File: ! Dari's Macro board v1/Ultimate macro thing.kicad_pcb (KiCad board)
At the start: 2 copper layers, 71 parts, among them J1 Conn_02x03_Odd_Even, J2 Conn_01x04, SW1 SW_Push, SW2 SW_Push, SW3 Rotary_Encoder, U1 ATmega328P-PU, Y1 16Mhz

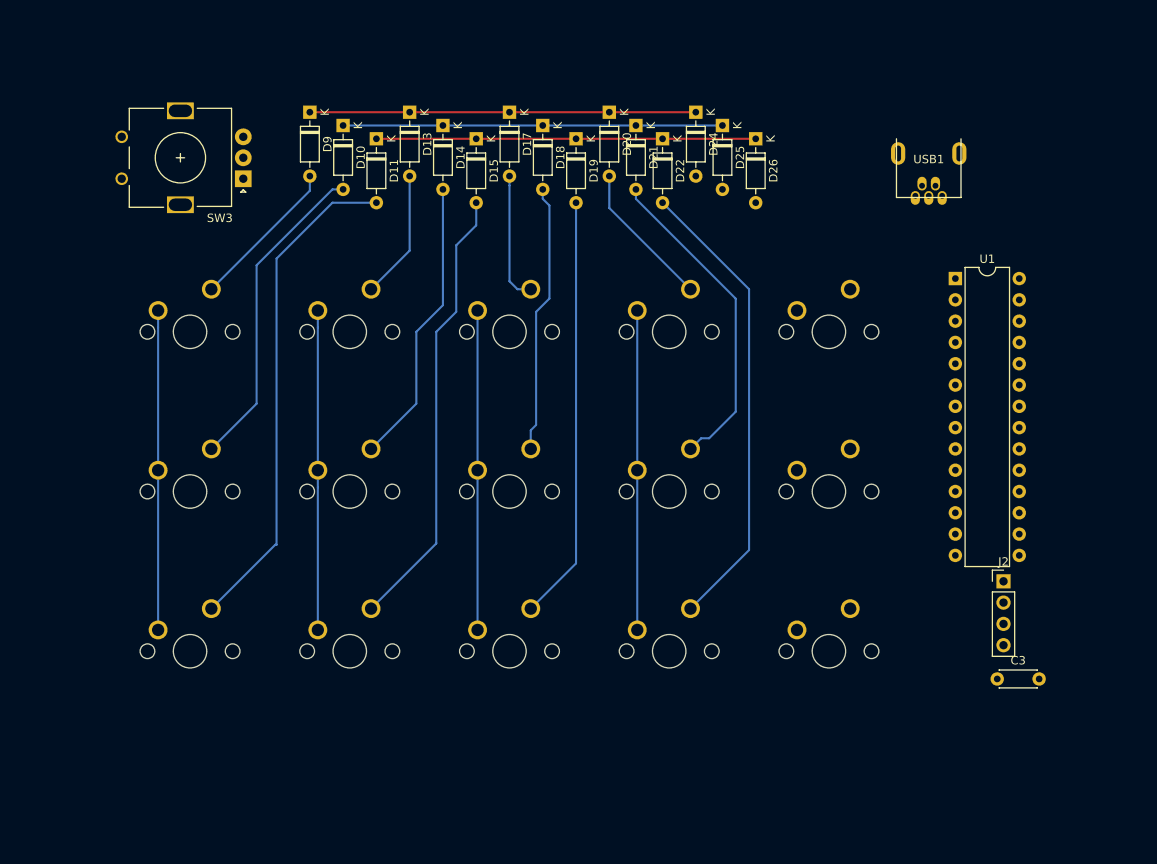
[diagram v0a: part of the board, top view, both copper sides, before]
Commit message: Linked encoder
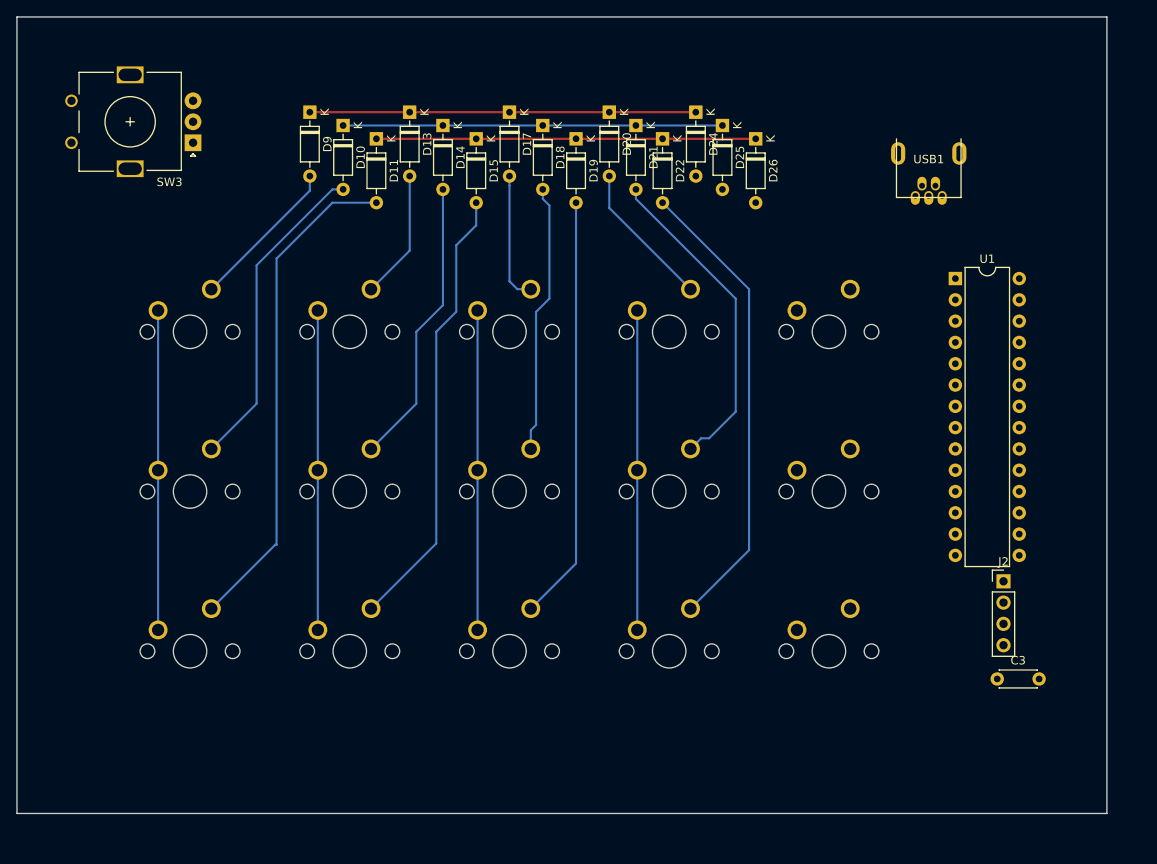
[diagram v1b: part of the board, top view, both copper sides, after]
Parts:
- moved SW3 7.37 mm to (71.0, 60.0)
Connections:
- SW3 pad A: Net-(SW3-PadA) -> ENC_A
- SW3 pad B: Net-(SW3-PadB) -> ENC_B
- SW3 pad C: Net-(SW3-PadC) -> ENC_C
- U1 pad 14: Net-(U1-Pad14) -> ENC_A
- U1 pad 15: Net-(U1-Pad15) -> ENC_C
- U1 pad 16: Net-(U1-Pad16) -> ENC_B
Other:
- board outline added: 130 x 95 mm
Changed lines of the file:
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@@
   (general
     (thickness 1.6)
-    (drawings 0)
+    (drawings 4)
     (tracks 72)
     (zones 0)
     (modules 71)
-    (nets 66)
+    (nets 63)
   )
   (page A4)
@@
     (solder_mask_min_width 0.25)
     (aux_axis_origin 0 0)
-    (visible_elements FFFFFF7F)
+    (visible_elements 7FFFFFFF)
     (pcbplotparams
       (layerselection 0x010fc_ffffffff)
@@
   (net 56 USB_D+)
   (net 57 "Net-(SW2-Pad1)")
-  (net 58 "Net-(SW3-PadA)")
-  (net 59 "Net-(SW3-PadC)")
-  (net 60 "Net-(SW3-PadB)")
-  (net 61 "Net-(U1-Pad14)")
-  (net 62 "Net-(U1-Pad21)")
-  (net 63 "Net-(U1-Pad16)")
-  (net 64 "Net-(U1-Pad15)")
-  (net 65 "Net-(USB1-Pad2)")
+  (net 58 "Net-(U1-Pad21)")
+  (net 59 "Net-(USB1-Pad2)")
+  (net 60 ENC_A)
+  (net 61 ENC_C)
+  (net 62 ENC_B)
   (net_class Default "This is the default net class."
     (clearance 0.2)
@@
     (add_net COL3)
     (add_net COL4)
+    (add_net ENC_A)
+    (add_net ENC_B)
+    (add_net ENC_C)
     (add_net GND)
     (add_net I2c_SCL)
@@
     (add_net "Net-(J1-Pad4)")
     (add_net "Net-(SW2-Pad1)")
-    (add_net "Net-(SW3-PadA)")
-    (add_net "Net-(SW3-PadB)")
-    (add_net "Net-(SW3-PadC)")
-    (add_net "Net-(U1-Pad14)")
-    (add_net "Net-(U1-Pad15)")
-    (add_net "Net-(U1-Pad16)")
     (add_net "Net-(U1-Pad21)")
     (add_net "Net-(USB1-Pad2)")
@@
       (net 6 "Net-(D2-Pad1)"))
     (pad 2 thru_hole oval (at 5.6 0.8 90) (size 1.65 1.1) (drill oval 0.7 (offset 0.25 0)) (layers *.Cu B.Mask)
-      (net 65 "Net-(USB1-Pad2)"))
+      (net 59 "Net-(USB1-Pad2)"))
     (pad 1 thru_hole oval (at 6.8 1.6 270) (size 1.65 1.1) (drill oval 0.7 (offset 0.25 0)) (layers *.Cu B.Mask)
       (net 1 GND))
@@
       (net 49 I2c_SCL))
     (pad 14 thru_hole oval (at 0 33.02) (size 1.6 1.6) (drill 0.8) (layers *.Cu *.Mask)
-      (net 61 "Net-(U1-Pad14)"))
+      (net 60 ENC_A))
     (pad 27 thru_hole oval (at 7.62 2.54) (size 1.6 1.6) (drill 0.8) (layers *.Cu *.Mask)
       (net 48 I2c_SDA))
@@
       (net 1 GND))
     (pad 21 thru_hole oval (at 7.62 17.78) (size 1.6 1.6) (drill 0.8) (layers *.Cu *.Mask)
-      (net 62 "Net-(U1-Pad21)"))
+      (net 58 "Net-(U1-Pad21)"))
     (pad 7 thru_hole oval (at 0 15.24) (size 1.6 1.6) (drill 0.8) (layers *.Cu *.Mask)
       (net 2 +5V))
@@
       (net 52 COL2))
     (pad 16 thru_hole oval (at 7.62 30.48) (size 1.6 1.6) (drill 0.8) (layers *.Cu *.Mask)
-      (net 63 "Net-(U1-Pad16)"))
+      (net 62 ENC_B))
     (pad 2 thru_hole oval (at 0 2.54) (size 1.6 1.6) (drill 0.8) (layers *.Cu *.Mask)
       (net 51 COL1))
     (pad 15 thru_hole oval (at 7.62 33.02) (size 1.6 1.6) (drill 0.8) (layers *.Cu *.Mask)
-      (net 64 "Net-(U1-Pad15)"))
+      (net 61 ENC_C))
     (pad 1 thru_hole rect (at 0 0) (size 1.6 1.6) (drill 0.8) (layers *.Cu *.Mask)
       (net 44 Reset))
@@
   )
   (module Rotary_Encoder:RotaryEncoder_Alps_EC11E_Vertical_H20mm (layer F.Cu)
-    (at 76.99375 64.29375 180)
+    (at 71 60 180)
     (descr "Alps rotary encoder, EC12E... without switch (pins are dummy), vertical shaft, http://www.alps.com/prod/info/E/HTML/Encoder/Incremental/EC11/EC11E15204A3.html")
     (tags "rotary encoder")
@@
     )
     (pad A thru_hole rect (at 0 0 180) (size 2 2) (drill 1) (layers *.Cu *.Mask)
-      (net 58 "Net-(SW3-PadA)"))
+      (net 60 ENC_A))
     (pad C thru_hole circle (at 0 2.5 180) (size 2 2) (drill 1) (layers *.Cu *.Mask)
-      (net 59 "Net-(SW3-PadC)"))
+      (net 61 ENC_C))
     (pad B thru_hole circle (at 0 5 180) (size 2 2) (drill 1) (layers *.Cu *.Mask)
-      (net 60 "Net-(SW3-PadB)"))
+      (net 62 ENC_B))
     (pad MP thru_hole rect (at 7.5 -3.1 180) (size 3.2 2) (drill oval 2.8 1.5) (layers *.Cu *.Mask))
     (pad MP thru_hole rect (at 7.5 8.1 180) (size 3.2 2) (drill oval 2.8 1.5) (layers *.Cu *.Mask))
@@
     )
   )
+  (gr_line (start 180 45) (end 180 140) (layer Edge.Cuts) (width 0.05))
+  (gr_line (start 50 140) (end 50 45) (layer Edge.Cuts) (width 0.05))
+  (gr_line (start 180 140) (end 50 140) (layer Edge.Cuts) (width 0.05))
+  (gr_line (start 50 45) (end 180 45) (layer Edge.Cuts) (width 0.05))
   (segment (start 84.93125 65.7225) (end 73.18375 77.47) (width 0.25) (layer B.Cu) (net 14))
   (segment (start 84.93125 63.97625) (end 84.93125 65.7225) (width 0.25) (layer B.Cu) (net 14))

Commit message: Redesign
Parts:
- removed D10, D11, D26, D9: 1N4148, Diode_THT:D_DO-35_SOD27_P7.62mm_Horizontal
- removed D12, D16, D27, D28, D29, D30, D31, D32, D33, D34, D8: WS2812B, LED_SMD:LED_WS2812B_PLCC4_5.0x5.0mm_P3.2mm
- added R10: 220, Resistor_THT:R_Axial_DIN0204_L3.6mm_D1.6mm_P5.08mm_Horizontal, F.Cu at (309.8, 229.9)
- added R9: 220, Resistor_THT:R_Axial_DIN0204_L3.6mm_D1.6mm_P5.08mm_Horizontal, F.Cu at (309.8, 226.8)
- D23, D7: value WS2812B -> 1N4148; footprint LED_SMD:LED_WS2812B_PLCC4_5.0x5.0mm_P3.2mm -> Diode_THT:D_DO-35_SOD27_P7.62mm_Horizontal
- D3: value WS2812B -> RED; footprint LED_SMD:LED_WS2812B_PLCC4_5.0x5.0mm_P3.2mm -> LED_THT:LED_D3.0mm_Clear
- D4: value WS2812B -> GREEN; footprint LED_SMD:LED_WS2812B_PLCC4_5.0x5.0mm_P3.2mm -> LED_THT:LED_D3.0mm_Clear
- D5: value RED -> 1N4148; footprint LED_THT:LED_D3.0mm_Clear -> Diode_THT:D_DO-35_SOD27_P7.62mm_Horizontal
- D6: value GREEN -> 1N4148; footprint LED_THT:LED_D3.0mm_Clear -> Diode_THT:D_DO-35_SOD27_P7.62mm_Horizontal
- MX10, MX12, MX14, MX3, MX4, MX8: footprint ! MX bases:MXOnly-1U-NoLED -> ! MX bases:MXOnly-1U
- moved D14 255.1 mm to (354.3, 86.9), turned to 0 degrees
- moved D15 226.1 mm to (323.3, 117.7), turned to 0 degrees
- moved D20 226.0 mm to (343.5, 94.0), turned to 0 degrees
- moved MX15 222.0 mm to (269.0, 287.0)
- moved D22 219.8 mm to (343.5, 97.5), turned to 0 degrees
- moved U1 216.1 mm to (289.0, 251.0)
- moved MX1 206.6 mm to (193.0, 249.0)
- moved MX4 206.6 mm to (212.0, 249.0)
- moved MX2 206.5 mm to (193.0, 268.0)
- moved MX7 206.5 mm to (231.0, 249.0)
- moved MX5 206.5 mm to (212.0, 268.0)
- moved MX3 206.5 mm to (193.0, 287.0)
- moved MX10 206.5 mm to (250.0, 249.0)
- moved MX8 206.5 mm to (231.0, 268.0)
- moved MX6 206.5 mm to (212.0, 287.0)
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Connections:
- D23 pad 1: +5V -> ROW0
- D24 pad 1: ROW0 -> ROW1
- D25 pad 1: ROW1 -> ROW2
- D3 pad 1: +5V -> GND
- D4 pad 1: +5V -> GND
- D5 pad 1: GND -> ROW0
- D6 pad 1: GND -> ROW1
- D7 pad 1: +5V -> ROW2
- J1 pad 3: Net-(J1-Pad3) -> ROW0
- MX1 pad 2: Net-(D9-Pad2) -> Net-(D5-Pad2)
- MX13 pad 2: Net-(D24-Pad2) -> Net-(D23-Pad2)
- MX14 pad 2: Net-(D25-Pad2) -> Net-(D24-Pad2)
- MX15 pad 2: Net-(D26-Pad2) -> Net-(D25-Pad2)
- MX2 pad 2: Net-(D10-Pad2) -> Net-(D6-Pad2)
- MX3 pad 2: Net-(D11-Pad2) -> Net-(D7-Pad2)
- R5 pad 1: Net-(D5-Pad2) -> Net-(D3-Pad2)
- R6 pad 1: Net-(D6-Pad2) -> Net-(D4-Pad2)
- U1 pad 19: Net-(J1-Pad3) -> ROW0
- U1 pad 23: ROW0 -> LED1
- U1 pad 6: RGBINPUT -> LED2
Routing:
- net Net-(D11-Pad2): track 59.7 -> 0.00 mm
- net Net-(D22-Pad2): track 55.6 -> 0.00 mm
- net Net-(D15-Pad2): track 53.6 -> 0.00 mm
- net Net-(D19-Pad2): track 50.7 -> 0.00 mm
- net ROW0: track 46.0 -> 0.00 mm
- net ROW2: track 45.2 -> 0.00 mm
- net ROW1: track 45.2 -> 0.00 mm
- net Net-(D21-Pad2): track 39.6 -> 0.00 mm
- net Net-(D10-Pad2): track 38.2 -> 0.00 mm
- net COL3: track 38.1 -> 0.00 mm
- net COL2: track 38.1 -> 0.00 mm
- net COL1: track 38.1 -> 0.00 mm
- net COL0: track 38.1 -> 0.00 mm
- net Net-(D14-Pad2): track 34.5 -> 0.00 mm
- net Net-(D18-Pad2): track 32.5 -> 0.00 mm
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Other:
- board outline removed

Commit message: Redesigned pro micro
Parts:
- removed R10: 220, Resistor_THT:R_Axial_DIN0204_L3.6mm_D1.6mm_P5.08mm_Horizontal
- added D10: 1N4148, Diode_THT:D_DO-35_SOD27_P7.62mm_Horizontal, F.Cu at (400.7, 417.6)
- added D11: 1N4148, Diode_THT:D_DO-35_SOD27_P7.62mm_Horizontal, F.Cu at (400.7, 414.1)
- added D12: 1N4148, Diode_THT:D_DO-35_SOD27_P7.62mm_Horizontal, F.Cu at (389.9, 421.2)
- added D16: 1N4148, Diode_THT:D_DO-35_SOD27_P7.62mm_Horizontal, F.Cu at (369.5, 425.4)
- added D26: 1N4148, Diode_THT:D_DO-35_SOD27_P7.62mm_Horizontal, F.Cu at (412.6, 424.7)
- added D27: 1N4148, Diode_THT:D_DO-35_SOD27_P7.62mm_Horizontal, F.Cu at (500.2, 336.8)
- added D28: 1N4148, Diode_THT:D_DO-35_SOD27_P7.62mm_Horizontal, F.Cu at (422.2, 414.1)
- added D29: WS2812B, LED_SMD:LED_WS2812B_PLCC4_5.0x5.0mm_P3.2mm, F.Cu at (480.2, 381.8)
- added D30: WS2812B, LED_SMD:LED_WS2812B_PLCC4_5.0x5.0mm_P3.2mm, F.Cu at (513.4, 351.1)
- added D31: WS2812B, LED_SMD:LED_WS2812B_PLCC4_5.0x5.0mm_P3.2mm, F.Cu at (500.4, 360.6)
- added D32: WS2812B, LED_SMD:LED_WS2812B_PLCC4_5.0x5.0mm_P3.2mm, F.Cu at (492.0, 358.6)
- added D33: WS2812B, LED_SMD:LED_WS2812B_PLCC4_5.0x5.0mm_P3.2mm, F.Cu at (460.0, 402.0)
- added D34: WS2812B, LED_SMD:LED_WS2812B_PLCC4_5.0x5.0mm_P3.2mm, F.Cu at (471.8, 378.8)
- added D35: WS2812B, LED_SMD:LED_WS2812B_PLCC4_5.0x5.0mm_P3.2mm, F.Cu at (451.6, 399.0)
- added D36: WS2812B, LED_SMD:LED_WS2812B_PLCC4_5.0x5.0mm_P3.2mm, F.Cu at (462.4, 395.4)
- added D37: WS2812B, LED_SMD:LED_WS2812B_PLCC4_5.0x5.0mm_P3.2mm, F.Cu at (451.6, 405.6)
- added D38: WS2812B, LED_SMD:LED_WS2812B_PLCC4_5.0x5.0mm_P3.2mm, F.Cu at (471.8, 385.4)
- added D39: WS2812B, LED_SMD:LED_WS2812B_PLCC4_5.0x5.0mm_P3.2mm, F.Cu at (492.0, 365.2)
- added D40: WS2812B, LED_SMD:LED_WS2812B_PLCC4_5.0x5.0mm_P3.2mm, F.Cu at (502.9, 354.0)
- added D41: WS2812B, LED_SMD:LED_WS2812B_PLCC4_5.0x5.0mm_P3.2mm, F.Cu at (482.6, 375.2)
- added D42: WS2812B, LED_SMD:LED_WS2812B_PLCC4_5.0x5.0mm_P3.2mm, F.Cu at (513.6, 344.5)
- added D43: WS2812B, LED_SMD:LED_WS2812B_PLCC4_5.0x5.0mm_P3.2mm, F.Cu at (435.6, 424.2)
- added D44: WS2812B, LED_SMD:LED_WS2812B_PLCC4_5.0x5.0mm_P3.2mm, F.Cu at (446.2, 415.6)
- added D45: WS2812B, LED_SMD:LED_WS2812B_PLCC4_5.0x5.0mm_P3.2mm, F.Cu at (454.6, 412.2)
- added D46: WS2812B, LED_SMD:LED_WS2812B_PLCC4_5.0x5.0mm_P3.2mm, F.Cu at (471.8, 392.0)
- added D47: WS2812B, LED_SMD:LED_WS2812B_PLCC4_5.0x5.0mm_P3.2mm, F.Cu at (492.0, 371.8)
- added D48: WS2812B, LED_SMD:LED_WS2812B_PLCC4_5.0x5.0mm_P3.2mm, F.Cu at (444.0, 424.2)
- added D49: WS2812B, LED_SMD:LED_WS2812B_PLCC4_5.0x5.0mm_P3.2mm, F.Cu at (500.4, 367.3)
- added D50: WS2812B, LED_SMD:LED_WS2812B_PLCC4_5.0x5.0mm_P3.2mm, F.Cu at (480.2, 388.5)
- added D51: WS2812B, LED_SMD:LED_WS2812B_PLCC4_5.0x5.0mm_P3.2mm, F.Cu at (508.9, 360.6)
- added D52: WS2812B, LED_SMD:LED_WS2812B_PLCC4_5.0x5.0mm_P3.2mm, F.Cu at (468.5, 402.0)
- added D8: 1N4148, Diode_THT:D_DO-35_SOD27_P7.62mm_Horizontal, F.Cu at (489.4, 353.5)
- added D9: 1N4148, Diode_THT:D_DO-35_SOD27_P7.62mm_Horizontal, F.Cu at (391.1, 424.7)
- added MX16: MX-NoLED, ! MX bases:MXOnly-1U-NoLED, F.Cu at (367.4, 341.6)
- added MX17: MX-NoLED, ! MX bases:MXOnly-1U-NoLED, F.Cu at (356.5, 399.0)
- added MX18: MX-NoLED, ! MX bases:MXOnly-1U-NoLED, F.Cu at (387.6, 341.6)
- added MX19: MX-NoLED, ! MX bases:MXOnly-1U-NoLED, F.Cu at (376.7, 361.8)
- added MX20: MX-NoLED, ! MX bases:MXOnly-1U-NoLED, F.Cu at (407.8, 341.6)
- added MX21: MX-NoLED, ! MX bases:MXOnly-1U-NoLED, F.Cu at (428.0, 341.6)
- added MX22: MX-NoLED, ! MX bases:MXOnly-1U-NoLED, F.Cu at (396.9, 361.8)
- added MX23: MX-NoLED, ! MX bases:MXOnly-1U-NoLED, F.Cu at (376.7, 382.0)
- added MX24: MX-NoLED, ! MX bases:MXOnly-1U-NoLED, F.Cu at (417.1, 361.8)
- MX10, MX12, MX14, MX3, MX4, MX8: footprint ! MX bases:MXOnly-1U -> ! MX bases:MXOnly-1U-NoLED
- R9: value 220 -> 470
- moved C2 345.2 mm to (423.4, 424.7)
- moved D4 341.6 mm to (449.9, 424.8)
- moved D5 341.1 mm to (411.4, 421.2)
- moved D2 339.3 mm to (401.8, 424.7)
- moved SW1 333.1 mm to (433.4, 414.3)
- moved D14 329.1 mm to (389.9, 414.1)
- moved D22 328.4 mm to (358.8, 425.6)
- moved D25 322.8 mm to (422.2, 417.6)
- moved D6 322.8 mm to (411.4, 417.6)
- moved R7 318.7 mm to (449.7, 420.5)
- moved R1 316.0 mm to (457.3, 406.9)
- moved D3 315.7 mm to (460.5, 411.3)
- moved R5 315.1 mm to (477.5, 393.3)
- moved R4 313.3 mm to (468.1, 396.9)
- moved D15 312.9 mm to (380.3, 425.4)
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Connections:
- net LED1 renamed RGBINPUT
- net Net-(J1-Pad1) renamed /COL5
- D20 pad 1: ROW0 -> /ROW3
- D21 pad 1: ROW1 -> ROW0
- D22 pad 1: ROW2 -> ROW1
- D23 pad 1: ROW0 -> ROW2
- D24 pad 1: ROW1 -> /ROW3
- D25 pad 1: ROW2 -> ROW0
- J1 pad 3: ROW0 -> /ROW3
- MX10 pad 1: COL3 -> COL2
- MX10 pad 2: Net-(D20-Pad2) -> Net-(D14-Pad2)
- MX11 pad 1: COL3 -> COL2
- MX11 pad 2: Net-(D21-Pad2) -> Net-(D15-Pad2)
- MX12 pad 1: COL3 -> COL2
- MX12 pad 2: Net-(D22-Pad2) -> Net-(D16-Pad2)
- MX13 pad 1: COL4 -> COL3
- MX13 pad 2: Net-(D23-Pad2) -> Net-(D17-Pad2)
- MX14 pad 1: COL4 -> COL3
- MX14 pad 2: Net-(D24-Pad2) -> Net-(D18-Pad2)
- MX15 pad 1: COL4 -> COL3
- MX15 pad 2: Net-(D25-Pad2) -> Net-(D19-Pad2)
- MX4 pad 1: COL1 -> COL0
- MX4 pad 2: Net-(D13-Pad2) -> Net-(D8-Pad2)
- MX5 pad 2: Net-(D14-Pad2) -> Net-(D9-Pad2)
- MX6 pad 2: Net-(D15-Pad2) -> Net-(D10-Pad2)
- MX7 pad 1: COL2 -> COL1
- MX7 pad 2: Net-(D17-Pad2) -> Net-(D11-Pad2)
- MX8 pad 1: COL2 -> COL1
- MX8 pad 2: Net-(D18-Pad2) -> Net-(D12-Pad2)
- MX9 pad 2: Net-(D19-Pad2) -> Net-(D13-Pad2)
- R9 pad 1: Net-(MX10-Pad3) -> Net-(D29-Pad4)
- U1 pad 19: ROW0 -> /ROW3
- U1 pad 6: LED2 -> ROW0

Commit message: a
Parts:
- moved SW3 235.4 mm to (334.0, 179.0), turned to 180 degrees
- moved D33 225.4 mm to (347.0, 207.0)
- moved D34 224.0 mm to (328.0, 207.0)
- moved MX13 209.8 mm to (385.0, 199.0)
- moved MX9 209.5 mm to (366.0, 199.0)
- moved MX5 209.2 mm to (347.0, 199.0)
- moved MX2 209.0 mm to (328.0, 218.0)
- moved MX17 205.5 mm to (404.0, 199.0)
- moved D32 197.1 mm to (366.0, 207.0)
- moved MX1 195.6 mm to (328.0, 199.0)
- moved MX3 194.9 mm to (328.0, 237.0)
- moved D31 192.2 mm to (385.0, 207.0)
- moved D29 184.0 mm to (423.0, 207.0)
- moved D36 181.1 mm to (404.0, 224.0)
- moved D30 181.0 mm to (404.0, 207.0)
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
